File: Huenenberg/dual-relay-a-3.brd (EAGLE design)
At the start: 77.5 x 50.8 mm, 38 parts, among them J1 12V, J10 REV, J11 NORM, J12 REV, J13 NORM, J14 REV, J15 NORM, J16 REV, J17 NORM, J18 CTRL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

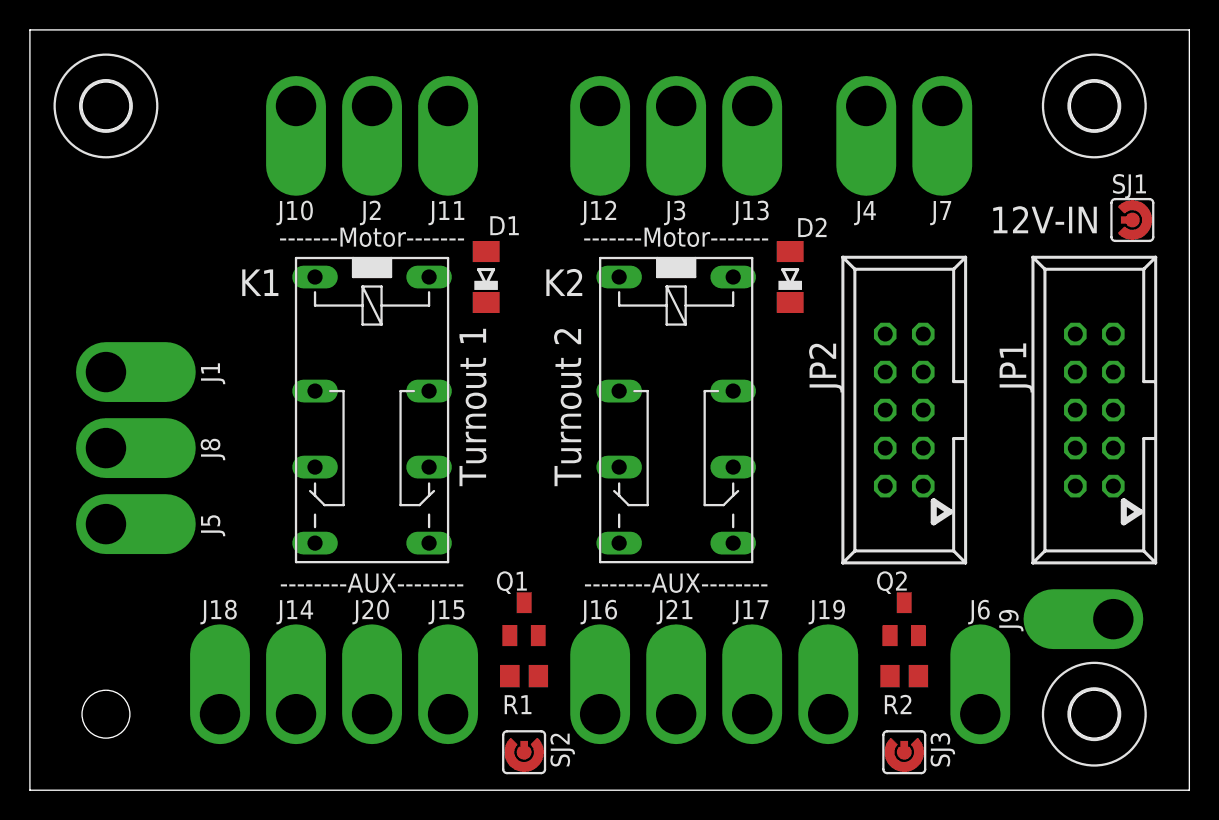
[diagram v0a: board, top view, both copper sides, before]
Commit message: Finishes routing of the turnout relay board.
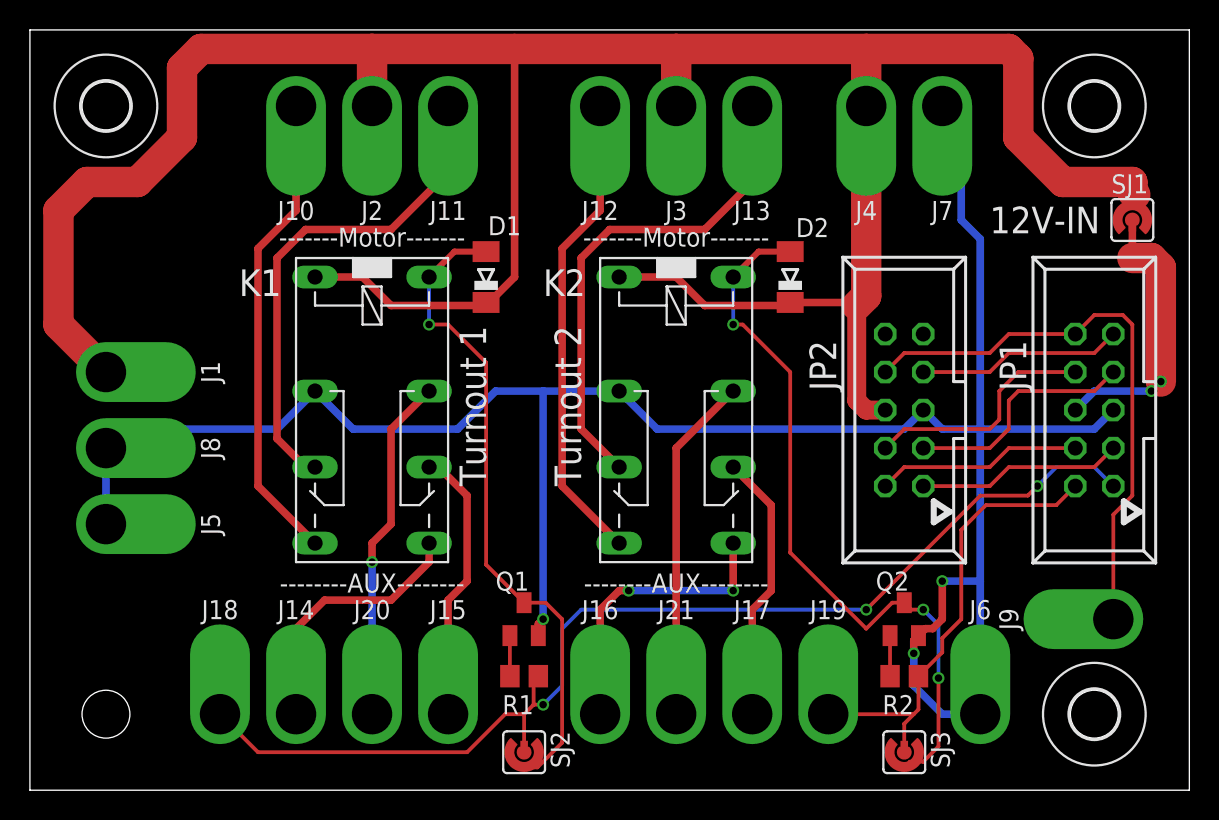
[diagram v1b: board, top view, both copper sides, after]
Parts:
- turned SJ1 to 90 degrees
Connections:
- removed net JN4: J5.P$1, J6.P$1, J7.P$1, J8.P$1
- net GND: now also J5.P$1, J6.P$1, J7.P$1, J8.P$1
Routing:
- net +12V: track 0.00 -> 181.5 mm
- net GND: track 0.00 -> 152.7 mm, vias 0 -> 3
- net N$2: track 0.00 -> 75.7 mm, vias 0 -> 3
- net N$9: track 0.00 -> 49.2 mm, vias 0 -> 3
- net N$1: track 0.00 -> 44.1 mm, vias 0 -> 1
- net N$22: track 0.00 -> 38.6 mm
- net N$5: track 0.00 -> 33.6 mm
- net N$13: track 0.00 -> 33.6 mm
- net N$4: track 0.00 -> 31.8 mm
- net N$12: track 0.00 -> 31.8 mm
- net N$18: track 0.00 -> 31.4 mm
- net N$8: track 0.00 -> 23.2 mm, vias 0 -> 1
- net N$16: track 0.00 -> 23.2 mm
- net N$14: track 0.00 -> 19.6 mm, vias 0 -> 2
- net +5V: track 0.00 -> 19.5 mm, vias 0 -> 2
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
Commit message: Adds some labels to make the IN/OUT more understandable. Renames some nets for the labels.
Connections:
- net N$18 renamed CTRL2
- net N$2 renamed CTRL1
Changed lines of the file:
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@@
 <setting verticaltext="up"/>
 </settings>
-<grid distance="25" unitdist="mil" unit="mil" style="lines" multiple="1" display="yes" altdistance="5" altunitdist="mil" altunit="mil"/>
+<grid distance="25" unitdist="mil" unit="mm" style="lines" multiple="1" display="yes" altdistance="5" altunitdist="mil" altunit="mil"/>
 <layers>
-<layer number="1" name="Top" color="4" fill="1" visible="yes" active="yes"/>
-<layer number="16" name="Bottom" color="1" fill="1" visible="yes" active="yes"/>
+<layer number="1" name="Top" color="4" fill="1" visible="no" active="yes"/>
+<layer number="16" name="Bottom" color="1" fill="1" visible="no" active="yes"/>
 <layer number="17" name="Pads" color="2" fill="1" visible="yes" active="yes"/>
 <layer number="18" name="Vias" color="2" fill="1" visible="yes" active="yes"/>
@@
 <wire x1="35.56" y1="3.175" x2="35.56" y2="11.43" width="0.254" layer="1"/>
 </signal>
-<signal name="N$2">
+<signal name="CTRL1">
 <contactref element="R1" pad="1"/>
 <contactref element="J18" pad="P$1"/>
@@
 <wire x1="74.93" y1="26.67" x2="75.565" y2="27.305" width="0.508" layer="16"/>
 </signal>
-<signal name="N$18">
+<signal name="CTRL2">
 <contactref element="JP1" pad="2"/>
 <contactref element="R2" pad="1"/>

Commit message: Adds ground planes and vias between ground planes.
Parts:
- flipped H3 to the top
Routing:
- net GND: vias 3 -> 52
- added copper zone on layer 1, net GND
- added copper zone on layer 16, net GND
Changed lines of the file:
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@@
 <setting verticaltext="up"/>
 </settings>
-<grid distance="25" unitdist="mil" unit="mm" style="lines" multiple="1" display="yes" altdistance="5" altunitdist="mil" altunit="mil"/>
+<grid distance="25" unitdist="mil" unit="mil" style="lines" multiple="1" display="yes" altdistance="5" altunitdist="mil" altunit="mil"/>
 <layers>
-<layer number="1" name="Top" color="4" fill="1" visible="no" active="yes"/>
-<layer number="16" name="Bottom" color="1" fill="1" visible="no" active="yes"/>
+<layer number="1" name="Top" color="4" fill="1" visible="yes" active="yes"/>
+<layer number="16" name="Bottom" color="1" fill="1" visible="yes" active="yes"/>
 <layer number="17" name="Pads" color="2" fill="1" visible="yes" active="yes"/>
 <layer number="18" name="Vias" color="2" fill="1" visible="yes" active="yes"/>
@@
 <layer number="26" name="bNames" color="7" fill="1" visible="yes" active="yes"/>
 <layer number="27" name="tValues" color="7" fill="1" visible="yes" active="yes"/>
-<layer number="28" name="bValues" color="7" fill="1" visible="yes" active="yes"/>
+<layer number="28" name="bValues" color="7" fill="1" visible="no" active="yes"/>
 <layer number="29" name="tStop" color="7" fill="3" visible="no" active="yes"/>
 <layer number="30" name="bStop" color="7" fill="6" visible="no" active="yes"/>
@@
 <layer number="41" name="tRestrict" color="4" fill="10" visible="yes" active="yes"/>
 <layer number="42" name="bRestrict" color="1" fill="10" visible="yes" active="yes"/>
-<layer number="43" name="vRestrict" color="2" fill="10" visible="yes" active="yes"/>
+<layer number="43" name="vRestrict" color="2" fill="10" visible="no" active="yes"/>
 <layer number="44" name="Drills" color="7" fill="1" visible="no" active="yes"/>
 <layer number="45" name="Holes" color="7" fill="1" visible="no" active="yes"/>
 <layer number="46" name="Milling" color="3" fill="1" visible="no" active="yes"/>
 <layer number="47" name="Measures" color="7" fill="1" visible="no" active="yes"/>
-<layer number="48" name="Document" color="7" fill="1" visible="yes" active="yes"/>
-<layer number="49" name="Reference" color="7" fill="1" visible="yes" active="yes"/>
+<layer number="48" name="Document" color="7" fill="1" visible="no" active="yes"/>
+<layer number="49" name="Reference" color="7" fill="1" visible="no" active="yes"/>
 <layer number="50" name="dxf" color="7" fill="1" visible="no" active="no"/>
 <layer number="51" name="tDocu" color="7" fill="1" visible="yes" active="yes"/>
@@
 <layer number="112" name="tSilk" color="7" fill="1" visible="no" active="yes"/>
 <layer number="113" name="ReferenceLS" color="7" fill="1" visible="no" active="no"/>
-<layer number="114" name="programming" color="7" fill="1" visible="yes" active="yes"/>
+<layer number="114" name="programming" color="7" fill="1" visible="no" active="yes"/>
 <layer number="116" name="Patch_BOT" color="9" fill="4" visible="no" active="yes"/>
 <layer number="118" name="Rect_Pads" color="7" fill="1" visible="no" active="no"/>
@@
 <layer number="131" name="tAdjust" color="7" fill="1" visible="no" active="yes"/>
 <layer number="132" name="bAdjust" color="7" fill="1" visible="no" active="yes"/>
-<layer number="144" name="Drill_legend" color="7" fill="1" visible="yes" active="yes"/>
+<layer number="144" name="Drill_legend" color="7" fill="1" visible="no" active="yes"/>
 <layer number="150" name="Notes" color="7" fill="1" visible="no" active="yes"/>
 <layer number="151" name="HeatSink" color="7" fill="1" visible="no" active="yes"/>
@@
 </element>
 <element name="Q1" library="eagleparts" package="SOT23" package3d_urn="urn:adsk.eagle:package:28738/2" value="MMBT3904" x="33.02" y="11.43" smashed="yes">
-<attribute name="NAME" x="31.115" y="13.335" size="1.27" layer="25"/>
+<attribute name="NAME" x="30.48" y="13.97" size="1.27" layer="25"/>
 <attribute name="VALUE" x="34.925" y="13.335" size="1.27" layer="27" rot="R90"/>
 </element>
@@
 <attribute name="POPULARITY" value="7" x="71.12" y="45.72" size="1.778" layer="27" display="off"/>
 </element>
-<element name="H3" library="holes" library_urn="urn:adsk.eagle:library:237" package="3,2" package3d_urn="urn:adsk.eagle:package:14275/1" value="MOUNT-HOLE3.2" x="5.08" y="5.08" smashed="yes" rot="MR0">
-<attribute name="POPULARITY" value="7" x="5.08" y="5.08" size="1.778" layer="28" rot="MR0" display="off"/>
+<element name="H3" library="holes" library_urn="urn:adsk.eagle:library:237" package="3,2" package3d_urn="urn:adsk.eagle:package:14275/1" value="MOUNT-HOLE3.2" x="5.08" y="5.08" smashed="yes">
+<attribute name="POPULARITY" value="7" x="5.08" y="5.08" size="1.778" layer="27" display="off"/>
 </element>
 <element name="H4" library="holes" library_urn="urn:adsk.eagle:library:237" package="3,2" package3d_urn="urn:adsk.eagle:package:14275/1" value="MOUNT-HOLE3.2" x="71.12" y="5.08" smashed="yes">
@@
 <wire x1="59.37" y1="10.33" x2="59.055" y2="10.015" width="0.508" layer="1"/>
 <wire x1="59.055" y1="10.015" x2="59.055" y2="9.144" width="0.508" layer="1"/>
-<via x="59.055" y="9.144" extent="1-16" drill="0.5"/>
+<via x="59.055" y="9.144" extent="1-16" drill="0.35"/>
 <wire x1="59.055" y1="9.144" x2="59.055" y2="6.985" width="0.508" layer="16"/>
 <wire x1="60.96" y1="5.08" x2="63.5" y2="5.08" width="0.508" layer="16"/>
@@
 <wire x1="16.51" y1="24.13" x2="6.35" y2="24.13" width="0.508" layer="16"/>
 <wire x1="5.08" y1="22.86" x2="5.08" y2="17.78" width="0.508" layer="16"/>
+<polygon width="0.0762" layer="1" isolate="0.254">
+<vertex x="0" y="50.8"/>
+<vertex x="77.47" y="50.8"/>
+<vertex x="77.47" y="0"/>
+<vertex x="0" y="0"/>
+</polygon>
+<polygon width="0.0762" layer="16" isolate="0.254">
+<vertex x="0" y="50.8"/>
+<vertex x="77.47" y="50.8"/>
+<vertex x="77.47" y="0"/>
+<vertex x="0" y="0"/>
+</polygon>
+<via x="8.255" y="35.56" extent="1-16" drill="0.35"/>
+<via x="13.335" y="45.085" extent="1-16" drill="0.35"/>
+<via x="1.27" y="49.53" extent="1-16" drill="0.35"/>
+<via x="11.43" y="33.655" extent="1-16" drill="0.35"/>
+<via x="1.905" y="10.795" extent="1-16" drill="0.35"/>
+<via x="9.525" y="10.795" extent="1-16" drill="0.35"/>
+<via x="10.16" y="1.905" extent="1-16" drill="0.35"/>
+<via x="29.845" y="1.27" extent="1-16" drill="0.35"/>
+<via x="43.18" y="1.27" extent="1-16" drill="0.35"/>
+<via x="64.77" y="1.27" extent="1-16" drill="0.35"/>
+<via x="76.2" y="1.27" extent="1-16" drill="0.35"/>
+<via x="76.2" y="12.065" extent="1-16" drill="0.35"/>
+<via x="76.2" y="24.13" extent="1-16" drill="0.35"/>
+<via x="76.2" y="39.37" extent="1-16" drill="0.35"/>
+<via x="76.2" y="49.53" extent="1-16" drill="0.35"/>
+<via x="59.69" y="37.465" extent="1-16" drill="0.35"/>
+<via x="68.58" y="37.465" extent="1-16" drill="0.35"/>
+<via x="63.5" y="31.115" extent="1-16" drill="0.35"/>
+<via x="61.595" y="26.035" extent="1-16" drill="0.35"/>
+<via x="68.58" y="24.13" extent="1-16" drill="0.35"/>
+<via x="54.61" y="17.78" extent="1-16" drill="0.35"/>
+<via x="48.895" y="24.13" extent="1-16" drill="0.35"/>
+<via x="41.91" y="29.845" extent="1-16" drill="0.35"/>
+<via x="33.655" y="24.13" extent="1-16" drill="0.35"/>
+<via x="31.75" y="30.48" extent="1-16" drill="0.35"/>
+<via x="27.94" y="24.13" extent="1-16" drill="0.35"/>
+<via x="33.655" y="15.24" extent="1-16" drill="0.35"/>
+<via x="41.91" y="14.605" extent="1-16" drill="0.35"/>
+<via x="45.085" y="18.415" extent="1-16" drill="0.35"/>
+<via x="40.005" y="24.13" extent="1-16" drill="0.35"/>
+<via x="39.37" y="19.05" extent="1-16" drill="0.35"/>
+<via x="26.67" y="19.05" extent="1-16" drill="0.35"/>
+<via x="19.685" y="19.05" extent="1-16" drill="0.35"/>
+<via x="20.32" y="10.795" extent="1-16" drill="0.35"/>
+<via x="13.97" y="15.875" extent="1-16" drill="0.35"/>
+<via x="19.05" y="24.13" extent="1-16" drill="0.35"/>
+<via x="18.415" y="30.48" extent="1-16" drill="0.35"/>
+<via x="34.925" y="39.37" extent="1-16" drill="0.35"/>
+<via x="29.845" y="38.735" extent="1-16" drill="0.35"/>
+<via x="40.64" y="38.735" extent="1-16" drill="0.35"/>
+<via x="46.355" y="36.195" extent="1-16" drill="0.35"/>
+<via x="52.07" y="40.005" extent="1-16" drill="0.35"/>
+<via x="50.165" y="30.48" extent="1-16" drill="0.35"/>
+<via x="65.405" y="16.51" extent="1-16" drill="0.35"/>
+<via x="71.12" y="19.05" extent="1-16" drill="0.35"/>
+<via x="73.66" y="33.02" extent="1-16" drill="0.35"/>
+<via x="59.055" y="17.78" extent="1-16" drill="0.35"/>
+<via x="52.07" y="25.4" extent="1-16" drill="0.35"/>
+<via x="50.8" y="13.97" extent="1-16" drill="0.35"/>
 </signal>
 <signal name="N$1">
@@
 <wire x1="46.99" y1="34.29" x2="48.69" y2="35.99" width="0.4064" layer="1"/>
 <wire x1="48.69" y1="35.99" x2="50.8" y2="35.99" width="0.4064" layer="1"/>
-<wire x1="58.42" y1="1.524" x2="58.801" y2="1.905" width="0.254" layer="1"/>
-<wire x1="58.801" y1="1.905" x2="59.69" y2="1.905" width="0.254" layer="1"/>
+<wire x1="58.42" y1="1.524" x2="59.055" y2="1.524" width="0.254" layer="1"/>
+<wire x1="59.436" y1="1.905" x2="59.055" y2="1.524" width="0.254" layer="1"/>
+<wire x1="59.436" y1="1.905" x2="59.69" y2="1.905" width="0.254" layer="1"/>
 <wire x1="59.69" y1="1.905" x2="60.706" y2="2.921" width="0.254" layer="1"/>
 <wire x1="60.706" y1="2.921" x2="60.706" y2="7.493" width="0.254" layer="1"/>
@@
 <mfgpreviewcolor name="substratecolor" color="0xFF786E46"/>
 </mfgpreviewcolors>
+<errors>
+</errors>
 </board>
 </drawing>
